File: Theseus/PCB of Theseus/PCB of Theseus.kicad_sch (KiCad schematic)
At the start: 47 parts, among them J1 Screw_Terminal_01x04, J2 Screw_Terminal_01x04, J4 Screw_Terminal_01x06, J7 Screw_Terminal_01x02, J8 Screw_Terminal_01x06, Q1 NMOS, Q2 NMOS, U1 TPS564257DRL, U2 MCP2562

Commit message: Theseus_Dev_Rev2
It's still the same PCB
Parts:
- removed C1, C5: 100nF, Capacitor_SMD:C_0603_1608Metric_Pad1.08x0.95mm_HandSolder, symbol Device:C_Small_US
- removed C18, C19: 0.1uF, Capacitor_SMD:C_0201_0603Metric_Pad0.64x0.40mm_HandSolder, symbol Device:C_Small_US
- removed C2, C24, C4: 22uF, Capacitor_SMD:C_0805_2012Metric_Pad1.18x1.45mm_HandSolder, symbol Device:C_Small_US
- removed C3: 10pF, Capacitor_SMD:C_0402_1005Metric_Pad0.74x0.62mm_HandSolder, symbol Device:C_Small_US
- removed C6: 10u, Capacitor_SMD:C_0603_1608Metric_Pad1.08x0.95mm_HandSolder, symbol Device:C_Small_US
- removed D1, D5: D, Diode_SMD:D_SMB-SMC_Universal_Handsoldering, symbol Device:D
- removed D3, D4: GREEN, Diode_SMD:D_0603_1608Metric_Pad1.05x0.95mm_HandSolder, symbol Device:LED
- removed H1, H2, H3, H4: ~, MountingHole:MountingHole_3.2mm_M3_Pad_Via, symbol Mechanical:MountingHole_Pad
- removed J1: Screw_Terminal_01x04, TerminalBlock_CUI:TerminalBlock_CUI_TB007-508-04_1x04_P5.08mm_Horizontal, symbol Connector:Screw_Terminal_01x04
- removed J4, J8: Screw_Terminal_01x06, TerminalBlock_CUI:TerminalBlock_CUI_TB007-508-06_1x06_P5.08mm_Horizontal, symbol Connector:Screw_Terminal_01x06
- removed Q1, Q2: NMOS, Package_TO_SOT_SMD:SOT-23-3, symbol Simulation_SPICE:NMOS
- removed R1, R2, R3: 150R, Resistor_SMD:R_0603_1608Metric_Pad0.98x0.95mm_HandSolder, symbol Device:R_Small_US
- removed R10: 10k, Resistor_SMD:R_0402_1005Metric_Pad0.72x0.64mm_HandSolder, symbol Device:R_Small_US
- removed R27, R28: 1k, Resistor_SMD:R_0402_1005Metric_Pad0.72x0.64mm_HandSolder, symbol Device:R_Small_US
- removed R4, R7: 169R, Resistor_SMD:R_0603_1608Metric_Pad0.98x0.95mm_HandSolder, symbol Device:R_Small_US
- removed R48, R49: 3.4k, Resistor_SMD:R_0402_1005Metric_Pad0.72x0.64mm_HandSolder, symbol Device:R_Small_US
- removed R5, R6: 150k, Resistor_SMD:R_0603_1608Metric_Pad0.98x0.95mm_HandSolder, symbol Device:R_Small_US
- removed R8: 221k, Resistor_SMD:R_0603_1608Metric_Pad0.98x0.95mm_HandSolder, symbol Device:R_Small_US
- removed R9: 30k, Resistor_SMD:R_0603_1608Metric_Pad0.98x0.95mm_HandSolder, symbol Device:R_Small_US
- removed U1: TPS564257DRL, Package_TO_SOT_SMD:SOT-563, symbol FYDP_Library:TPS564257DRL
- added C1, C25, C32, C6: 10u, Capacitor_SMD:C_0805_2012Metric_Pad1.18x1.45mm_HandSolder, symbol Device:C
- added C2, C3: 100n, Capacitor_SMD:C_0805_2012Metric_Pad1.18x1.45mm_HandSolder, symbol Device:C
- added C24, C4, C5: 22u, Capacitor_SMD:C_0805_2012Metric_Pad1.18x1.45mm_HandSolder, symbol Device:C
- added H5, H6, H7, H8: MountingHole, MountingHole:MountingHole_4.3mm_M4, symbol Mechanical:MountingHole
- added TP10: TestPoint, TestPoint:TestPoint_Pad_D2.0mm, symbol Connector:TestPoint
- added U1: TPS565201DDC, Package_TO_SOT_SMD:SOT-23-6_Handsoldering, symbol FYDP_Library:TPS565201DDC
- F1: value TBD -> 3.5A 0685T3500-01
- J2: value Screw_Terminal_01x04 -> TB001-500-04BE
- J7: value Screw_Terminal_01x02 -> TB002-500-02BE
- L1: value 3.3uH -> 2.2u; footprint Fydp_footprints:VLS6045EX-3R3N -> Fydp_footprints:SPM6530T-2R2M
- R11: value 45.3k -> 33.2k; footprint Resistor_SMD:R_0603_1608Metric_Pad0.98x0.95mm_HandSolder -> Resistor_SMD:R_0805_2012Metric_Pad1.20x1.40mm_HandSolder; symbol Device:R_Small_US -> Device:R_US
- R12: value 10k -> 10.2k; footprint Resistor_SMD:R_0402_1005Metric_Pad0.72x0.64mm_HandSolder -> Resistor_SMD:R_0805_2012Metric_Pad1.20x1.40mm_HandSolder; symbol Device:R_Small_US -> Device:R_US
- R46: value 30K -> 3M ±1%; footprint Resistor_SMD:R_0603_1608Metric_Pad0.98x0.95mm_HandSolder -> Resistor_SMD:R_0805_2012Metric_Pad1.20x1.40mm_HandSolder; symbol Device:R_Small_US -> Device:R_US
- R47: value 10K -> 1M ±0.1%; footprint Resistor_SMD:R_0402_1005Metric_Pad0.72x0.64mm_HandSolder -> Resistor_SMD:R_0805_2012Metric_Pad1.20x1.40mm_HandSolder; symbol Device:R_Small_US -> Device:R_US
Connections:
- net +3.3V: now also C24.1, C25.1, C4.1, C5.1
- net +5V: now also C6.1
- net +BATT: now also C1.1, C2.1, C32.1, U1.3 (VIN), U1.5 (EN)
- net GND: now also C1.2, C2.2, C24.2, C25.2, C32.2, C4.2, C5.2, C6.2, TP10.1, U1.1 (GND)
- net at L1.2: now also C3.1, U1.2 (SW)
- net at R11.2, R12.1: now also U1.4 (VFB)
- new net: C3.2, U1.6 (VBST)
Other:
- sheet RTD renamed Temperature Sensors
- added sheet Valves and Sensors (untitled.kicad_sch)
- sheet MCU ports: added TC1_NSS, TC1_SCK, TC1_SI, TC2+, TC2-, TC3; removed RTD_1, RTD_2, RTD_3
- sheet Temperature Sensors ports: added TC1_CS, TC1_SCK, TC1_SO, TC2+, TC2-, TC3; removed RTD1, RTD2, RTD3
- note added: "Battery Connector"
- note added: "Converter 10.5-12.7V to 3.3V, 2A max, from https://webench.ti.com/appinfo/webench/scripts/SDP.cgi?ID=52AAB47309F73FFC"
- note removed: "1x 0.1uF per Hall sensor"
- note removed: "Converter 10.5-12.6V to 3.3V, 2A max, from https://webench.ti.com/appinfo/webench/scripts/SDP.cgi?ID=4A6C29459A6BA209"
- note removed: "Hall Sensor Connector"
- note removed: "Pressure Transducer Connector"
- note removed: "Scaling 4-20 mA to 0.6-3V"
- note removed: "Using pull down resistors so that valves start closed always"
- note removed: "Valve Connector"
- moved on the sheet: F1, J2, J7, L1, U2

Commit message: Flight design, first pass
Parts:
- removed J2: TB001-500-04BE, TerminalBlock_CUI:TerminalBlock_CUI_TB007-508-04_1x04_P5.08mm_Horizontal, symbol Connector:Screw_Terminal_01x04
- added J3: G125-MH104M4-04AD000P, canhw_footprints:connector_Harwin_G125-MH104M4-04AD000P, symbol canhw:G125-MH104M4-04AD000P
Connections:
- net +5V: now also J3.C (+5V)
- net CANH: now also J3.1 (CANH)
- net CANL: now also J3.2 (CANL)
- net GND: now also J3.D (GND)
- no-connect marks 0 -> 4
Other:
- removed sheet Temperature Sensors
- sheet MCU ports: added none; removed TC2+, TC2-, TC3
- sheet Valves and Sensors ports: added TC1_CS, TC1_SCK, TC1_SO; removed none

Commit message: Flight design v1
First pass at flight design
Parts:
- C1, C2, C24, C25, C3, C32, C4, C5, C6: footprint Capacitor_SMD:C_0805_2012Metric_Pad1.18x1.45mm_HandSolder -> Capacitor_SMD:C_0603_1608Metric_Pad1.08x0.95mm_HandSolder
- J7: value TB002-500-02BE -> 4DB-P108-02; footprint TerminalBlock_CUI:TerminalBlock_CUI_TB007-508-02_1x02_P5.08mm_Horizontal -> canhw_footprints:4DB-P108-02
- R11, R12: footprint Resistor_SMD:R_0805_2012Metric_Pad1.20x1.40mm_HandSolder -> Resistor_SMD:R_0603_1608Metric_Pad0.98x0.95mm_HandSolder
- R46: value 3M ±1% -> 300K; footprint Resistor_SMD:R_0805_2012Metric_Pad1.20x1.40mm_HandSolder -> Resistor_SMD:R_0603_1608Metric_Pad0.98x0.95mm_HandSolder
- R47: value 1M ±0.1% -> 100K; footprint Resistor_SMD:R_0805_2012Metric_Pad1.20x1.40mm_HandSolder -> Resistor_SMD:R_0603_1608Metric_Pad0.98x0.95mm_HandSolder
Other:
- sheet MCU ports: added PT4, PT5, PT6; removed none
- sheet Valves and Sensors ports: added PT4, PT5, PT6; removed none
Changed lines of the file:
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@@
 	(text "Max 12.6V, Divide-by-4 gives 3.15V"
 		(exclude_from_sim no)
-		(at 211.074 39.37 0)
+		(at 205.74 37.338 0)
 		(effects
 			(font
@@
 	(wire
 		(pts
+			(xy 212.09 138.43) (xy 231.14 138.43)
+		)
+		(stroke
+			(width 0)
+			(type default)
+		)
+	)
+	(wire
+		(pts
 			(xy 212.09 74.93) (xy 231.14 74.93)
 		)
@@
 	(wire
 		(pts
+			(xy 212.09 146.05) (xy 231.14 146.05)
+		)
+		(stroke
+			(width 0)
+			(type default)
+		)
+	)
+	(wire
+		(pts
 			(xy 114.3 106.68) (xy 114.3 99.06)
 		)
@@
 	(wire
 		(pts
+			(xy 212.09 142.24) (xy 231.14 142.24)
+		)
+		(stroke
+			(width 0)
+			(type default)
+		)
+	)
+	(wire
+		(pts
 			(xy 212.09 106.68) (xy 231.14 106.68)
 		)
@@
 			)
 		)
-		(property "Footprint" "Capacitor_SMD:C_0805_2012Metric_Pad1.18x1.45mm_HandSolder"
+		(property "Footprint" "Capacitor_SMD:C_0603_1608Metric_Pad1.08x0.95mm_HandSolder"
 			(at 133.0452 161.29 0)
 			(effects
@@
 			)
 		)
-		(property "Value" "1M ±0.1%"
+		(property "Value" "100K"
 			(at 168.91 43.1799 0)
 			(effects
@@
 			)
 		)
-		(property "Footprint" "Resistor_SMD:R_0805_2012Metric_Pad1.20x1.40mm_HandSolder"
+		(property "Footprint" "Resistor_SMD:R_0603_1608Metric_Pad0.98x0.95mm_HandSolder"
 			(at 167.386 42.164 90)
 			(effects
@@
 			)
 		)
-		(property "Footprint" "Capacitor_SMD:C_0805_2012Metric_Pad1.18x1.45mm_HandSolder"
+		(property "Footprint" "Capacitor_SMD:C_0603_1608Metric_Pad1.08x0.95mm_HandSolder"
 			(at 67.0052 113.03 0)
 			(effects
@@
 			)
 		)
-		(property "Footprint" "Capacitor_SMD:C_0805_2012Metric_Pad1.18x1.45mm_HandSolder"
+		(property "Footprint" "Capacitor_SMD:C_0603_1608Metric_Pad1.08x0.95mm_HandSolder"
 			(at 85.09 150.1648 0)
 			(effects
@@
 			)
 		)
-		(property "Footprint" "Capacitor_SMD:C_0805_2012Metric_Pad1.18x1.45mm_HandSolder"
+		(property "Footprint" "Capacitor_SMD:C_0603_1608Metric_Pad1.08x0.95mm_HandSolder"
 			(at 25.0952 160.02 0)
 			(effects
@@
 			)
 		)
-		(property "Footprint" "Capacitor_SMD:C_0805_2012Metric_Pad1.18x1.45mm_HandSolder"
+		(property "Footprint" "Capacitor_SMD:C_0603_1608Metric_Pad1.08x0.95mm_HandSolder"
 			(at 121.6152 161.29 0)
 			(effects
@@
 			)
 		)
-		(property "Value" "3M ±1%"
+		(property "Value" "300K"
 			(at 168.91 30.4799 0)
 			(effects
@@
 			)
 		)
-		(property "Footprint" "Resistor_SMD:R_0805_2012Metric_Pad1.20x1.40mm_HandSolder"
+		(property "Footprint" "Resistor_SMD:R_0603_1608Metric_Pad0.98x0.95mm_HandSolder"
 			(at 167.386 29.464 90)
 			(effects
@@
 			)
 		)
-		(property "Footprint" "Capacitor_SMD:C_0805_2012Metric_Pad1.18x1.45mm_HandSolder"
+		(property "Footprint" "Capacitor_SMD:C_0603_1608Metric_Pad1.08x0.95mm_HandSolder"
 			(at 144.4752 161.29 0)
 			(effects
@@
 			)
 		)
-		(property "Footprint" "Capacitor_SMD:C_0805_2012Metric_Pad1.18x1.45mm_HandSolder"
+		(property "Footprint" "Capacitor_SMD:C_0603_1608Metric_Pad1.08x0.95mm_HandSolder"
 			(at 56.8452 113.03 0)
 			(effects
@@
 			)
 		)
-		(property "Value" "TB002-500-02BE"
+		(property "Value" "4DB-P108-02"
 			(at 198.12 26.6699 0)
 			(effects
@@
 			)
 		)
-		(property "Footprint" "TerminalBlock_CUI:TerminalBlock_CUI_TB007-508-02_1x02_P5.08mm_Horizontal"
+		(property "Footprint" "canhw_footprints:4DB-P108-02"
 			(at 195.58 24.13 0)
 			(effects
@@
 			)
 		)
-		(property "Footprint" "Capacitor_SMD:C_0805_2012Metric_Pad1.18x1.45mm_HandSolder"
+		(property "Footprint" "Capacitor_SMD:C_0603_1608Metric_Pad1.08x0.95mm_HandSolder"
 			(at 47.9552 160.02 0)
 			(effects
@@
 			)
 		)
-		(property "Footprint" "Resistor_SMD:R_0805_2012Metric_Pad1.20x1.40mm_HandSolder"
+		(property "Footprint" "Resistor_SMD:R_0603_1608Metric_Pad0.98x0.95mm_HandSolder"
 			(at 110.236 151.384 90)
 			(effects
@@
 			)
 		)
-		(property "Footprint" "Resistor_SMD:R_0805_2012Metric_Pad1.20x1.40mm_HandSolder"
+		(property "Footprint" "Resistor_SMD:R_0603_1608Metric_Pad0.98x0.95mm_HandSolder"
 			(at 110.236 164.084 90)
 			(effects
@@
 			)
 		)
-		(property "Footprint" "Capacitor_SMD:C_0805_2012Metric_Pad1.18x1.45mm_HandSolder"
+		(property "Footprint" "Capacitor_SMD:C_0603_1608Metric_Pad1.08x0.95mm_HandSolder"
 			(at 36.5252 160.02 0)
 			(effects
@@
 	(sheet
 		(at 231.14 91.44)
-		(size 20.32 44.45)
+		(size 20.32 60.96)
 		(exclude_from_sim no)
 		(in_bom yes)
@@
 		)
 		(property "Sheetfile" "untitled.kicad_sch"
-			(at 231.14 136.4746 0)
+			(at 231.14 152.9846 0)
 			(effects
 				(font
@@
 			)
 		)
+		(pin "PT4" input
+			(at 231.14 138.43 180)
+			(effects
+				(font
+					(size 1.27 1.27)
+				)
+				(justify left)
+			)
+		)
+		(pin "PT5" input
+			(at 231.14 142.24 180)
+			(effects
+				(font
+					(size 1.27 1.27)
+				)
+				(justify left)
+			)
+		)
+		(pin "PT6" input
+			(at 231.14 146.05 180)
+			(effects
+				(font
+					(size 1.27 1.27)
+				)
+				(justify left)
+			)
+		)
 		(instances
 			(project "PCB of Theseus"
@@
 	(sheet
 		(at 165.1 54.61)
-		(size 46.99 78.74)
+		(size 46.99 99.06)
 		(exclude_from_sim no)
 		(in_bom yes)
@@
 		)
 		(property "Sheetfile" "mcu.kicad_sch"
-			(at 165.1 133.9346 0)
+			(at 165.1 154.2546 0)
 			(effects
 				(font
@@
 			(effects
 				(font
+					(size 1.27 1.27)
+				)
+				(justify right)
+			)
+		)
+		(pin "PT4" input
+			(at 212.09 138.43 0)
+			(effects
+				(font
+					(size 1.27 1.27)
+				)
+				(justify right)
+			)
+		)
+		(pin "PT5" input
+			(at 212.09 142.24 0)
+			(effects
+				(font
+					(size 1.27 1.27)
+				)
+				(justify right)
+			)
+		)
+		(pin "PT6" input
+			(at 212.09 146.05 0)
+			(effects
+				(font

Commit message: 10 MAR 2026 Changes pt 2
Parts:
- C25, C6: value 10u -> 0.1u
- R12: value 10.2k -> 10k
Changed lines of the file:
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@@
 			)
 		)
-		(property "Value" "10u"
+		(property "Value" "0.1u"
 			(at 59.944 110.49 0)
 			(effects
@@
 			)
 		)
-		(property "Value" "10u"
+		(property "Value" "0.1u"
 			(at 49.53 110.49 0)
 			(effects
@@
 			)
 		)
-		(property "Value" "10.2k"
+		(property "Value" "10k"
 			(at 111.76 165.0999 0)
 			(effects

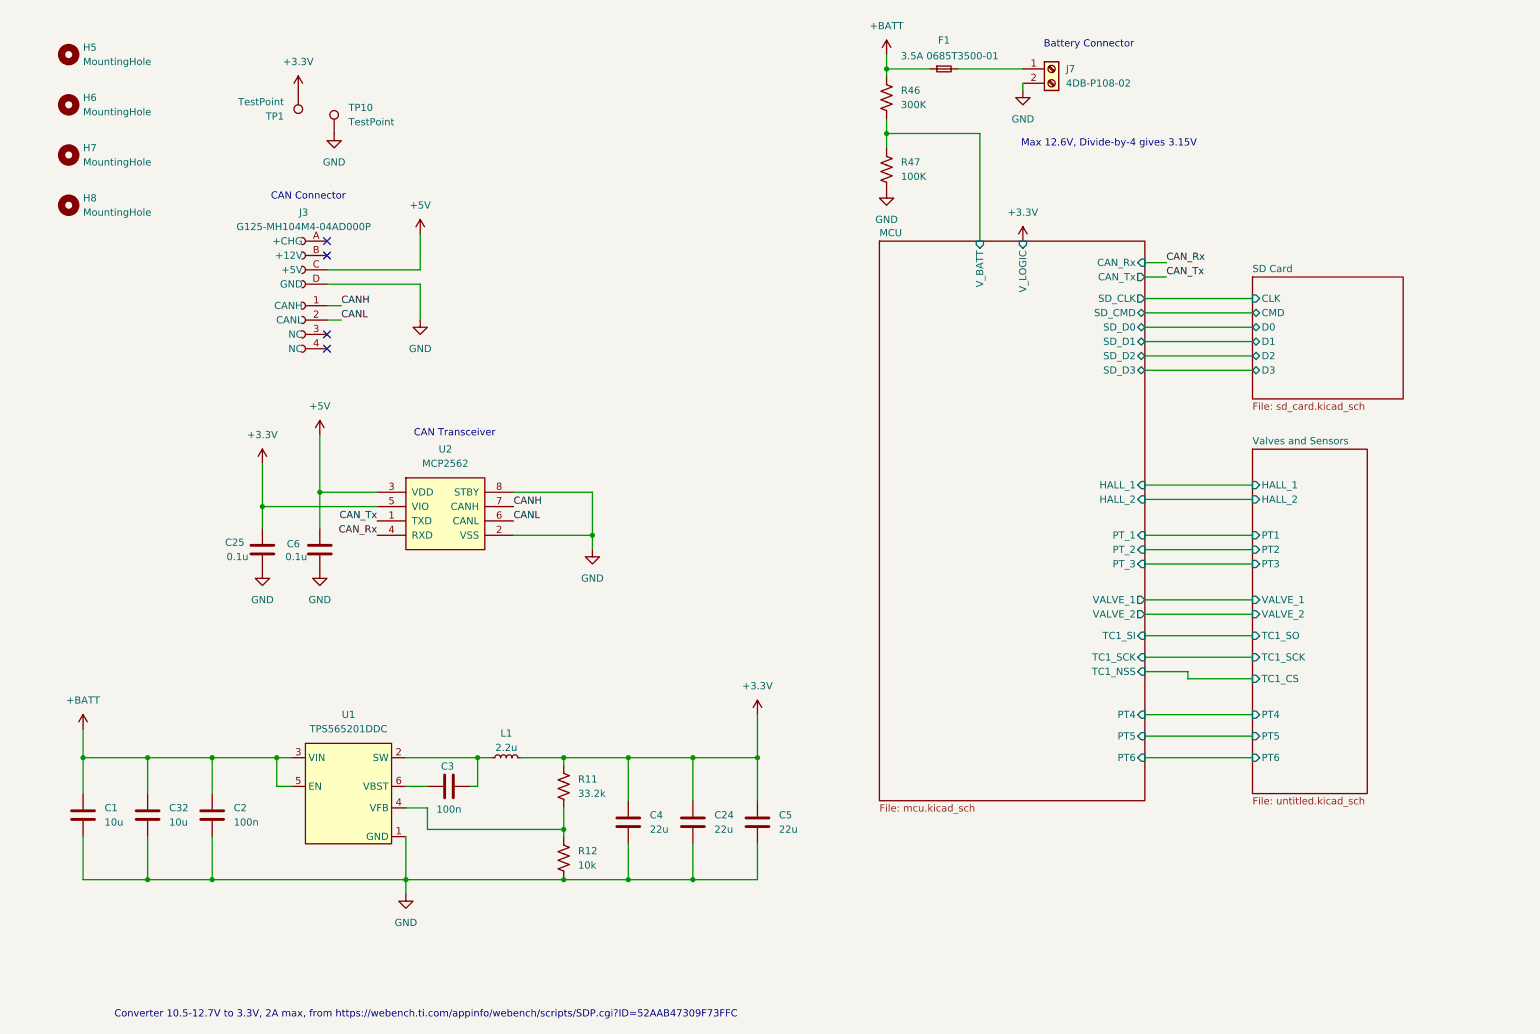
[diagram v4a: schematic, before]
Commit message: change CAN transciever to 3v3, add lipo charging, change PT connectors, tidy schematic
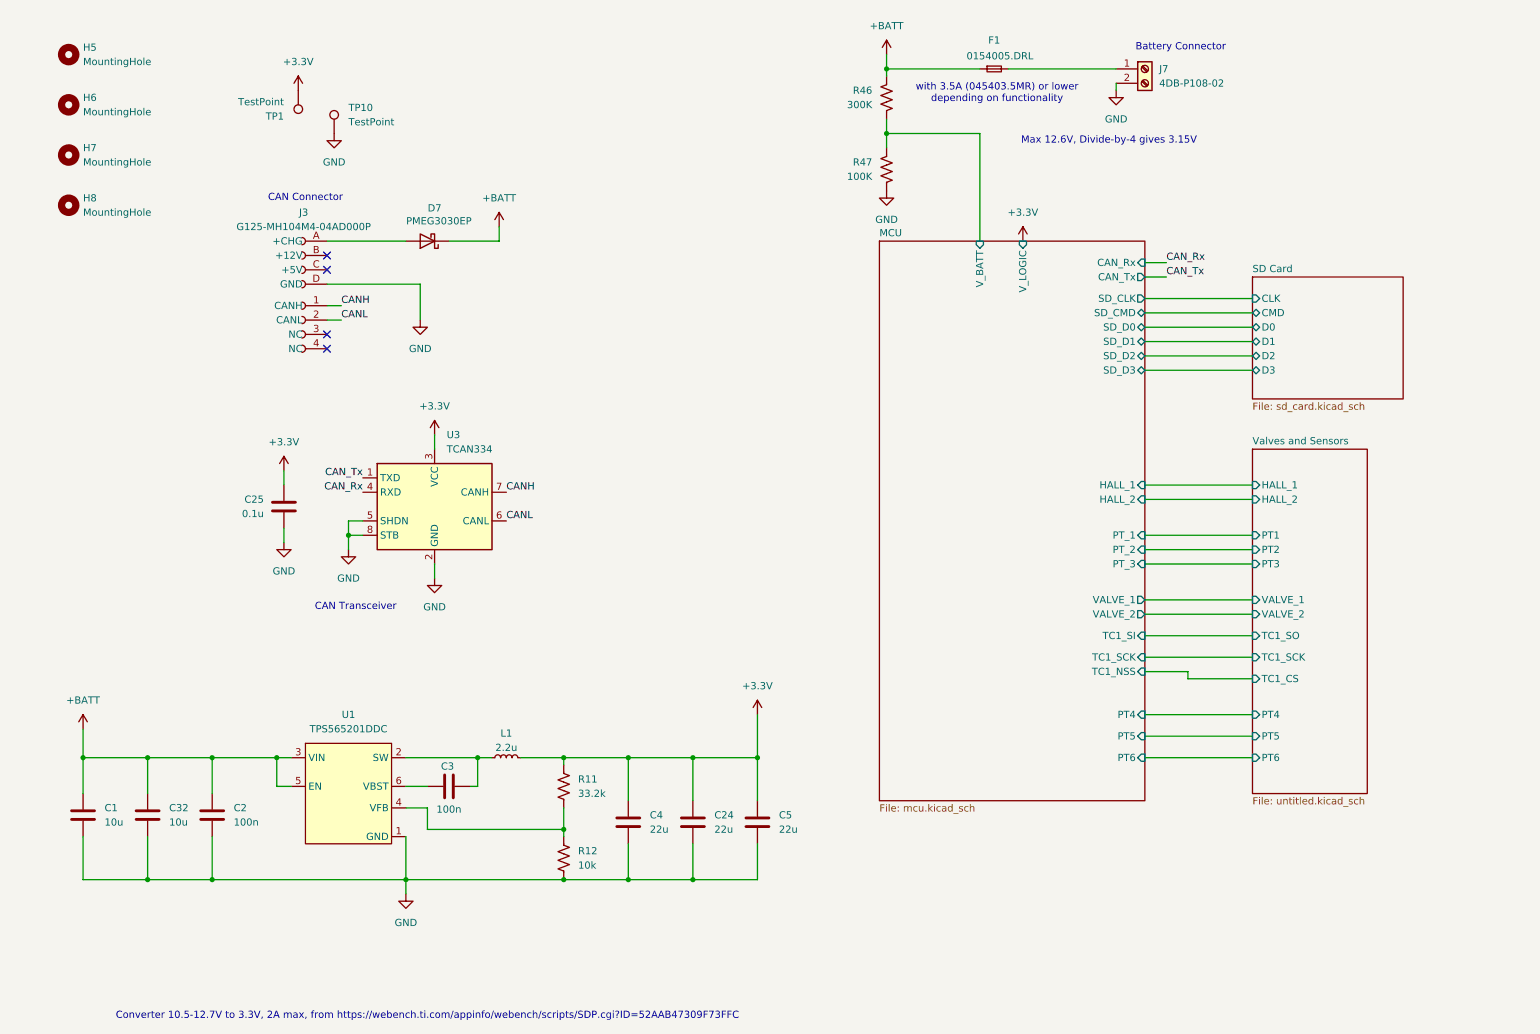
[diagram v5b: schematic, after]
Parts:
- removed C6: 0.1u, Capacitor_SMD:C_0603_1608Metric_Pad1.08x0.95mm_HandSolder, symbol Device:C
- removed U2: MCP2562, Package_SO:SOIC-8_3.9x4.9mm_P1.27mm, symbol canhw:MCP2562
- added D7: PMEG3030EP, Diode_SMD:D_SOD-128, symbol Device:D_Schottky
- added U3: TCAN334, Package_SO:SOIC-8_3.9x4.9mm_P1.27mm, symbol Interface_CAN_LIN:TCAN334
- F1: value 3.5A 0685T3500-01 -> 0154005.DRL; footprint Fuse:Fuse_1206_3216Metric_Pad1.42x1.75mm_HandSolder -> Fydp_footprints:FUSE_0154005.DR
- TP10: footprint TestPoint:TestPoint_Pad_D2.0mm -> TestPoint:TestPoint_Keystone_5000-5004_Miniature
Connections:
- net +3.3V: now also U3.3 (VCC)
- net +BATT: now also D7.1 (K)
- net CANH: now also U3.7 (CANH)
- net CANL: now also U3.6 (CANL)
- net CAN_Rx: now also U3.4 (RXD)
- net CAN_Tx: now also U3.1 (TXD)
- net GND: now also U3.2 (GND), U3.5 (SHDN), U3.8 (STB)
- net at J3.A (+CHG): now also D7.2 (A)
- net +5V: no longer names the net of J3.C (+5V)
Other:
- note added: "with 3.5A (045403.5MR) or lower depending on functionality"
- moved on the sheet: C25, F1, J7
